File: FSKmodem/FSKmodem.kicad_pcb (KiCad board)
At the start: 2 copper layers, 27.6 x 14.6 mm, 9 parts, among them IC1 TCM3105, Q1 CSTLS_G

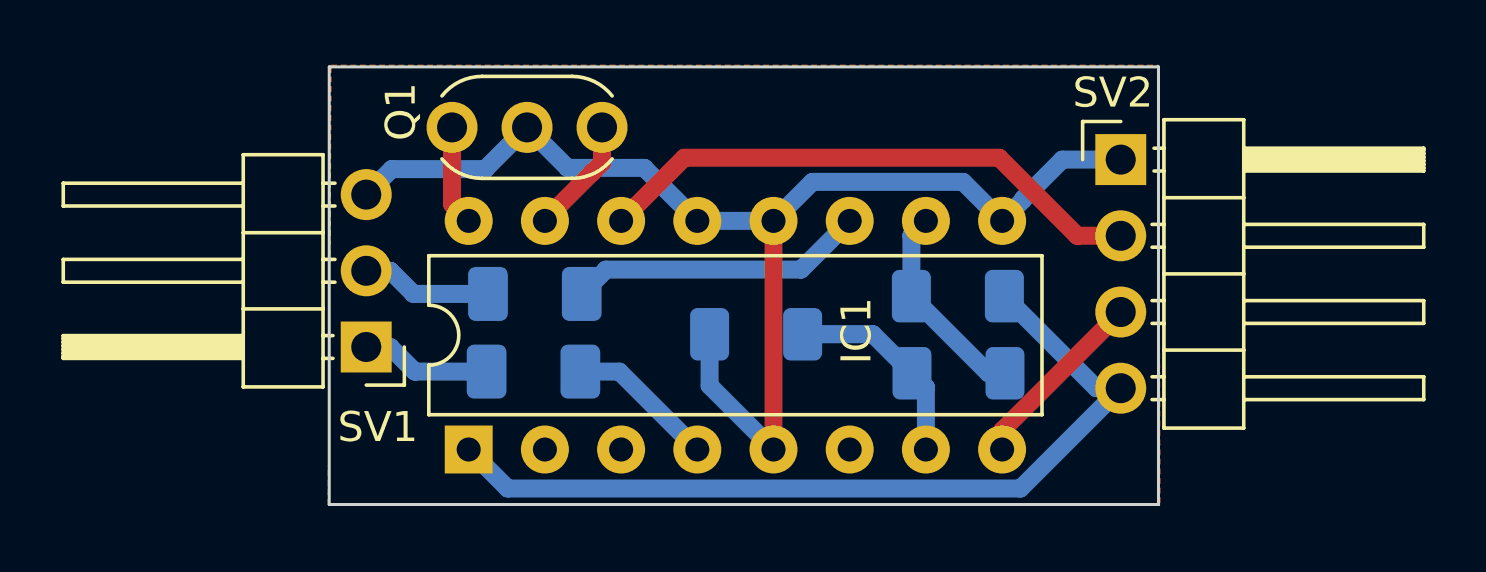
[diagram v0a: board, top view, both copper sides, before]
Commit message: change zone filling
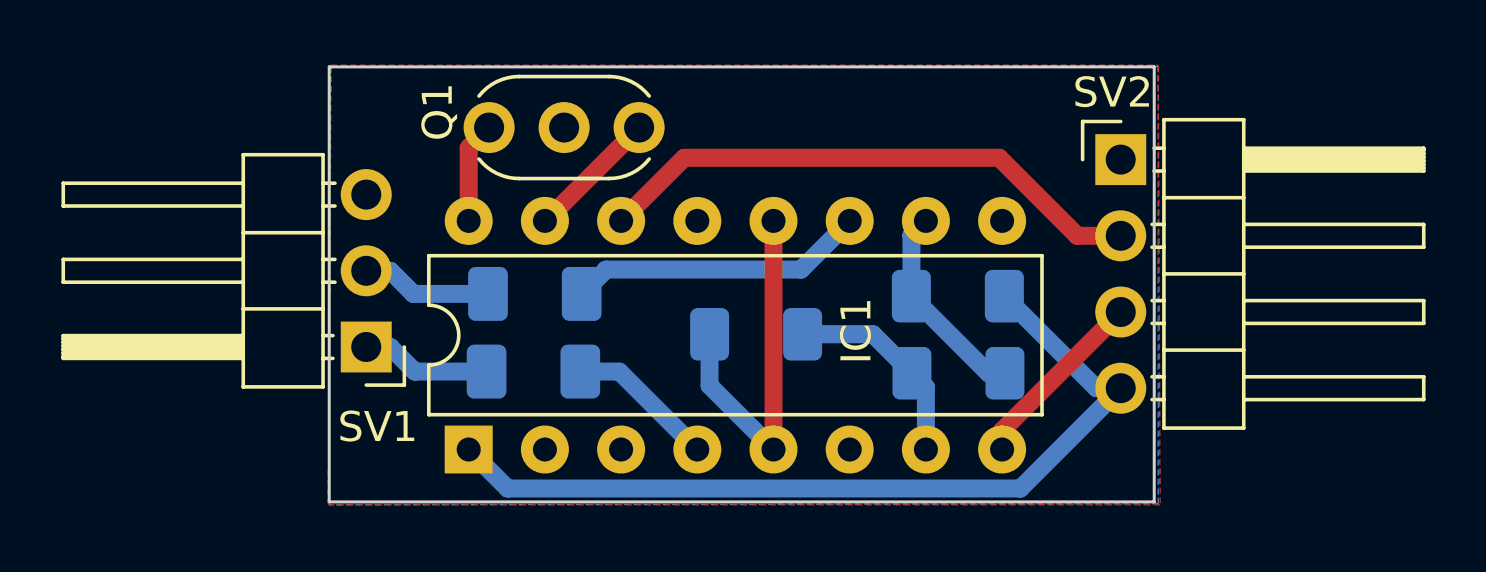
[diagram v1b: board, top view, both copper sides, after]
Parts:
- moved Q1 1.24 mm to (112.9, 66.2)
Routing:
- net GND: track 41.7 -> 12.3 mm
- net Net-(IC1-OSC1): track 3.91 -> 4.43 mm
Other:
- board size 27.6 x 14.6 mm -> 27.5 x 14.5 mm
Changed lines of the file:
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@@
   )
   (setup
+    (stackup
+      (layer "F.SilkS" (type "Top Silk Screen"))
+      (layer "F.Paste" (type "Top Solder Paste"))
+      (layer "F.Mask" (type "Top Solder Mask") (thickness 0.01))
+      (layer "F.Cu" (type "copper") (thickness 0.035))
+      (layer "dielectric 1" (type "core") (thickness 1.51) (material "FR4") (epsilon_r 4.5) (loss_tangent 0.02))
+      (layer "B.Cu" (type "copper") (thickness 0.035))
+      (layer "B.Mask" (type "Bottom Solder Mask") (thickness 0.01))
+      (layer "B.Paste" (type "Bottom Solder Paste"))
+      (layer "B.SilkS" (type "Bottom Silk Screen"))
+      (copper_finish "None")
+      (dielectric_constraints no)
+    )
     (pad_to_mask_clearance 0)
     (pcbplotparams
@@
     (property "Sheetfile" "FSKmodem.kicad_sch")
     (property "Sheetname" "")
-    (attr through_hole)
+    (attr through_hole allow_missing_courtyard)
     (fp_text reference "SV2" (at -0.263141 -2.229951) (layer "F.SilkS")
         (effects (font (size 1 1) (thickness 0.15)))
@@
   )
   (footprint "Crystal:Resonator-3Pin_W6.0mm_H3.0mm" (layer "F.Cu")
-    (at 111.6856 66.2085 180)
+    (at 112.920606 66.213256 180)
     (descr "Ceramic Resomator/Filter 6.0x3.0mm^2, length*width=6.0x3.0mm^2 package, package length=6.0mm, package width=3.0mm, 3 pins")
     (tags "THT ceramic resonator filter")
@@
     (property "Sheetname" "")
     (attr smd)
-    (fp_text reference "R3" (at 0 1.82 -360) (layer "B.SilkS") hide
+    (fp_text reference "R3" (at 0 1.82 -360) (layer "B.SilkS")
         (effects (font (size 1 1) (thickness 0.15)) (justify mirror))
     )
@@
     )
   )
-  (gr_rect (start 102.591201 64.192051) (end 130.233012 78.779296)
+  (gr_rect (start 102.591201 64.192051) (end 130.091201 78.692051)
     (stroke (width 0.1) (type default)) (fill none) (layer "Edge.Cuts"))
   (segment (start 112.2645 74.3494) (end 114.8609 76.9458) (width 0.6) (layer "B.Cu") (net 1))
@@
   (segment (start 108.5409 78.2458) (end 125.6317 78.2458) (width 0.6) (layer "B.Cu") (net 5))
   (segment (start 117.4009 76.9458) (end 117.4009 69.3258) (width 0.6) (layer "F.Cu") (net 8))
-  (segment (start 104.67548 67.598788) (end 107.795312 67.598788) (width 0.6) (layer "B.Cu") (net 8))
   (segment (start 115.270319 73.10468) (end 115.270319 74.815219) (width 0.6) (layer "B.Cu") (net 8))
-  (segment (start 118.7009 68.0258) (end 123.7209 68.0258) (width 0.6) (layer "B.Cu") (net 8))
-  (segment (start 125.0209 69.3258) (end 125.73 68.6167) (width 0.6) (layer "B.Cu") (net 8))
-  (segment (start 123.7209 68.0258) (end 125.0209 69.3258) (width 0.6) (layer "B.Cu") (net 8))
-  (segment (start 117.4009 69.3258) (end 118.7009 68.0258) (width 0.6) (layer "B.Cu") (net 8))
-  (segment (start 110.5356 67.5585) (end 113.0936 67.5585) (width 0.6) (layer "B.Cu") (net 8))
-  (segment (start 113.0936 67.5585) (end 114.8609 69.3258) (width 0.6) (layer "B.Cu") (net 8))
-  (segment (start 125.73 68.58) (end 127.0275 67.2825) (width 0.6) (layer "B.Cu") (net 8))
-  (segment (start 125.73 68.6167) (end 125.73 68.58) (width 0.6) (layer "B.Cu") (net 8))
-  (segment (start 109.1856 66.2085) (end 110.5356 67.5585) (width 0.6) (layer "B.Cu") (net 8))
-  (segment (start 127.0275 67.2825) (end 128.975 67.2825) (width 0.6) (layer "B.Cu") (net 8))
-  (segment (start 107.795312 67.598788) (end 109.1856 66.2085) (width 0.6) (layer "B.Cu") (net 8))
-  (segment (start 114.8609 69.3258) (end 117.4009 69.3258) (width 0.6) (layer "B.Cu") (net 8))
   (segment (start 115.270319 74.815219) (end 117.4009 76.9458) (width 0.6) (layer "B.Cu") (net 8))
-  (segment (start 103.82548 68.448788) (end 104.67548 67.598788) (width 0.6) (layer "B.Cu") (net 8))
   (segment (start 118.370319 73.10468) (end 120.715352 73.10468) (width 0.6) (layer "B.Cu") (net 10))
   (segment (start 122.4809 76.9458) (end 122.4809 74.870228) (width 0.6) (layer "B.Cu") (net 10))
@@
   (segment (start 114.4249 67.2218) (end 112.3209 69.3258) (width 0.6) (layer "F.Cu") (net 13))
   (segment (start 127.525 69.8225) (end 124.9243 67.2218) (width 0.6) (layer "F.Cu") (net 13))
-  (segment (start 111.6856 67.386121) (end 111.6856 66.2085) (width 0.6) (layer "F.Cu") (net 14))
-  (segment (start 109.7809 69.2891) (end 111.372955 67.697045) (width 0.6) (layer "F.Cu") (net 14))
-  (segment (start 109.7809 69.3258) (end 109.7809 69.2891) (width 0.6) (layer "F.Cu") (net 14))
-  (segment (start 111.374676 67.697045) (end 111.6856 67.386121) (width 0.6) (layer "F.Cu") (net 14))
-  (segment (start 111.372955 67.697045) (end 111.374676 67.697045) (width 0.6) (layer "F.Cu") (net 14))
-  (segment (start 106.6856 68.7705) (end 107.2409 69.3258) (width 0.6) (layer "F.Cu") (net 15))
-  (segment (start 106.6856 66.2085) (end 106.6856 68.7705) (width 0.6) (layer "F.Cu") (net 15))
+  (segment (start 109.808062 69.3258) (end 112.920606 66.213256) (width 0.6) (layer "F.Cu") (net 14))
+  (segment (start 109.7809 69.3258) (end 109.808062 69.3258) (width 0.6) (layer "F.Cu") (net 14))
+  (segment (start 107.2409 69.3258) (end 107.2409 66.892962) (width 0.6) (layer "F.Cu") (net 15))
+  (segment (start 107.2409 66.892962) (end 107.920606 66.213256) (width 0.6) (layer "F.Cu") (net 15))
   (zone (net 8) (net_name "GND") (layer "F.Cu") (hatch edge 0.5)
     (connect_pads (clearance 0.5))

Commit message: ready for lut
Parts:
- moved C2 7.40 mm to (116.8, 71.7)
- moved R1 7.21 mm to (116.8, 74.5), turned to 180 degrees
- moved R3 6.99 mm to (123.7, 71.7)
- moved SV1 1.02 mm to (103.8, 74.6)
- moved SV2 0.91 mm to (129.0, 68.2)
- moved C1 0.32 mm to (109.1, 74.5)
- moved R2 0.21 mm to (123.7, 74.5), turned to 180 degrees
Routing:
- net GND: track 12.3 -> 66.2 mm
- net Net-(C2-Pad2): track 4.38 -> 11.6 mm
- net Net-(IC1-TXA): track 9.94 -> 2.97 mm
- net +5V: track 28.8 -> 34.5 mm
- net Net-(IC1-CDL): track 6.89 -> 9.59 mm
- net Net-(IC1-RXD): track 6.22 -> 5.49 mm
- net Net-(IC1-TXD): track 18.6 -> 19.2 mm
- net Net-(C1-Pad2): track 4.35 -> 3.80 mm
- removed copper zone on B.Cu, net GND
- removed copper zone on F.Cu, net GND
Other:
- board size 27.5 x 14.5 mm -> 27.9 x 15 mm
